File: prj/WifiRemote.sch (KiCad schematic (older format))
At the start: 68 parts, among them J1 DIP-BLACK-MALE-HEADER-VERT_4P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, J2 DIP-BLACK-MALE-HEADER_6P-2.54_, K1 DIP-SWITCH-TACTILE-SPST-NO_TS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, K2 DIP-SWITCH-TACTILE-SPST-NO_TS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, K3 DIP-SWITCH-TACTILE-SPST-NO_TS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, K4 DIP-SWITCH-TACTILE-SPST-NO_TS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, M1 Mechanical_Mount, M2 Mechanical_Mount, M3 Mechanical_Mount, M4 Mechanical_Mount, Q1 SMD-MOSFET-P-CH-20V-2A-FDN340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, SW1 DIP-TOGGLE-SWITCH-ON-ON_3+2P-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, U1 CONTROLLER-ESP8266, U2 BOOST-MCP1642B-ADJI/MC-MSOP8

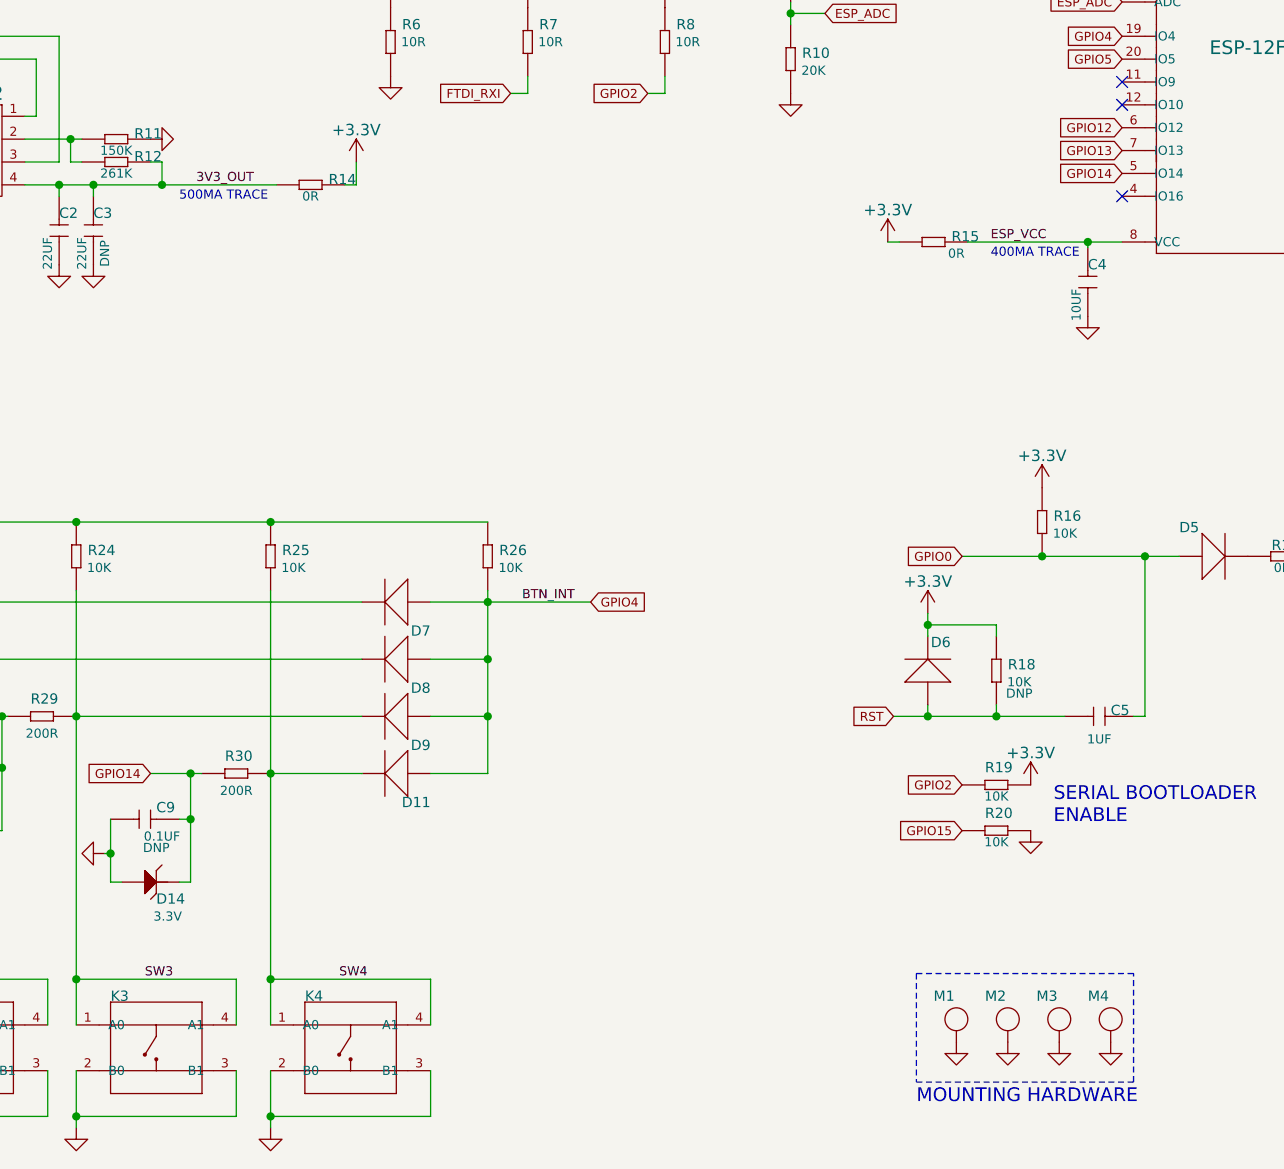
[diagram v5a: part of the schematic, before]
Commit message: Added mounting hole footprint
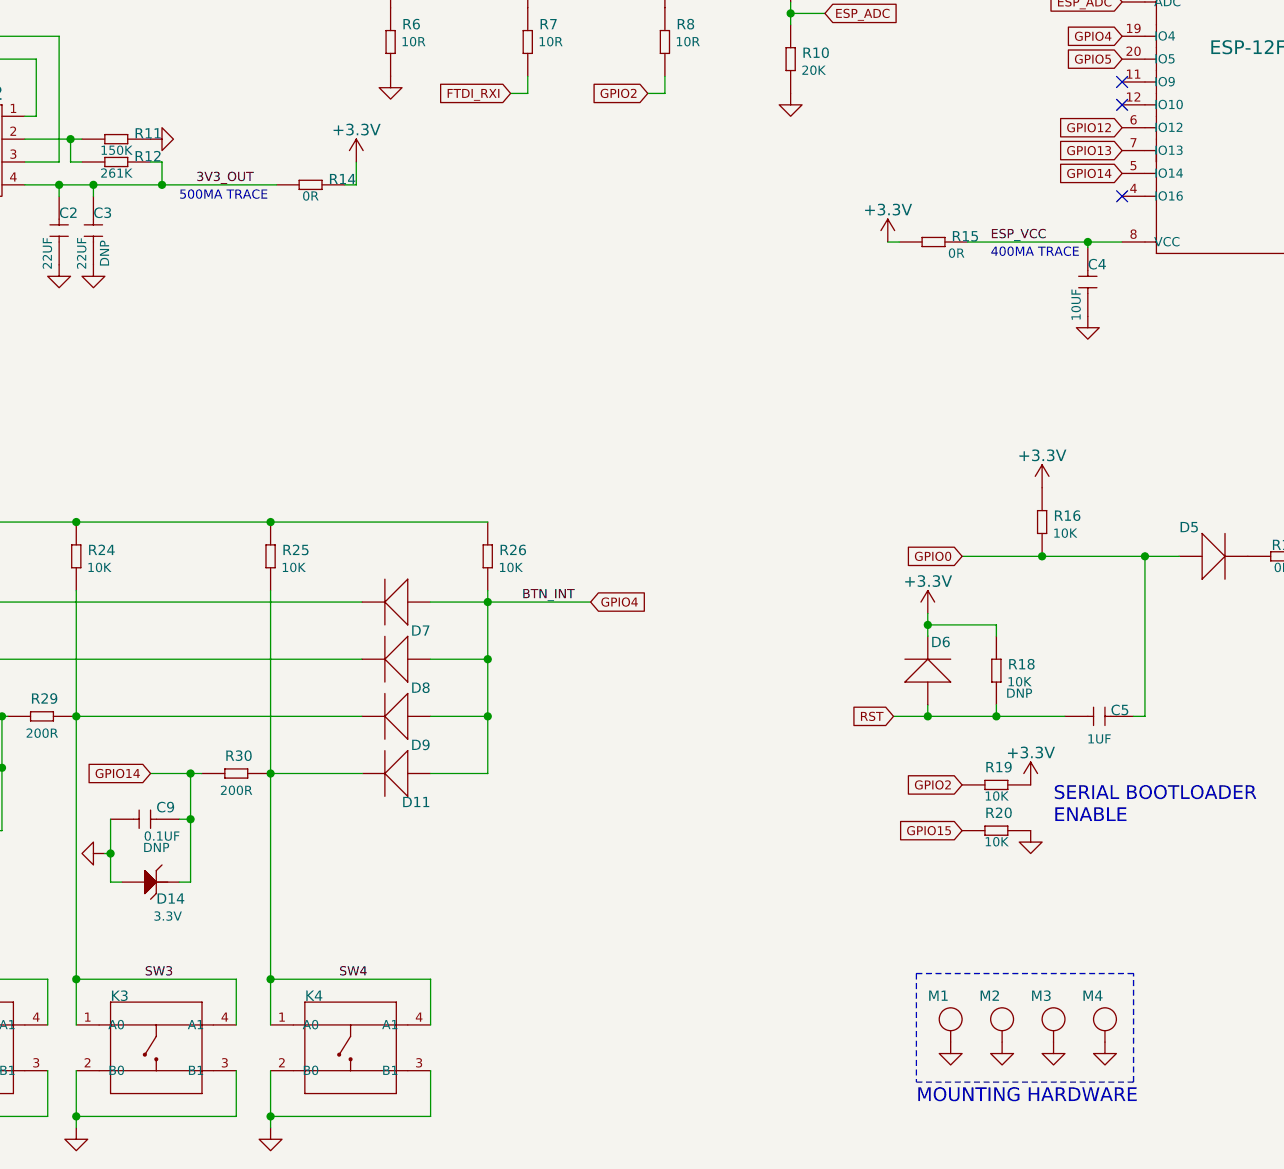
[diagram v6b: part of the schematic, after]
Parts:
- M1, M2, M3, M4: footprint (none) -> ICEE-Mechanical:mounting_panhead6
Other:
- moved on the sheet: M1, M2, M3, M4
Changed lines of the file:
@@
 	3750 2050 3800 2050
 Wire Wire Line
-	3800 2150 3800 2050
+	3800 2050 3800 2150
 Wire Wire Line
 	3500 2150 3500 2200
@@
 L Mechanical_Mount M1
 U 1 1 59BB9484
-P 7275 5800
-F 0 "M1" H 7175 5875 45  0000 L BNN
-F 1 "Mechanical_Mount" H 7075 5600 45  0001 L BNN
-F 2 "" H 7275 5800 60  0001 C CNN
-F 3 "" H 7275 5800 60  0001 C CNN
-	1    7275 5800
+P 7250 5800
+F 0 "M1" H 7150 5875 45  0000 L BNN
+F 1 "Mechanical_Mount" H 7050 5600 45  0001 L BNN
+F 2 "ICEE-Mechanical:mounting_panhead6" H 7250 5800 60  0001 C CNN
+F 3 "" H 7250 5800 60  0001 C CNN
+	1    7250 5800
 	1    0    0    -1
 $EndComp
@@
 L Mechanical_Mount M2
 U 1 1 59BB9AA5
-P 7500 5800
-F 0 "M2" H 7400 5875 45  0000 L BNN
-F 1 "Mechanical_Mount" H 7300 5600 45  0001 L BNN
-F 2 "" H 7500 5800 60  0001 C CNN
-F 3 "" H 7500 5800 60  0001 C CNN
-	1    7500 5800
+P 7475 5800
+F 0 "M2" H 7375 5875 45  0000 L BNN
+F 1 "Mechanical_Mount" H 7275 5600 45  0001 L BNN
+F 2 "ICEE-Mechanical:mounting_panhead6" H 7475 5800 60  0001 C CNN
+F 3 "" H 7475 5800 60  0001 C CNN
+	1    7475 5800
 	1    0    0    -1
 $EndComp
@@
 L Mechanical_Mount M3
 U 1 1 59BB9B95
-P 7725 5800
-F 0 "M3" H 7625 5875 45  0000 L BNN
-F 1 "Mechanical_Mount" H 7525 5600 45  0001 L BNN
-F 2 "" H 7725 5800 60  0001 C CNN
-F 3 "" H 7725 5800 60  0001 C CNN
-	1    7725 5800
-	1    0    0    -1
-$EndComp
-$Comp
-L GNDD #PWR?
+P 7700 5800
+F 0 "M3" H 7600 5875 45  0000 L BNN
+F 1 "Mechanical_Mount" H 7500 5600 45  0001 L BNN
+F 2 "ICEE-Mechanical:mounting_panhead6" H 7700 5800 60  0001 C CNN
+F 3 "" H 7700 5800 60  0001 C CNN
+	1    7700 5800
+	1    0    0    -1
+$EndComp
+$Comp
+L GNDD #PWR037
 U 1 1 59BC0554
-P 7275 5900
-F 0 "#PWR?" H 7275 5650 50  0001 C CNN
-F 1 "GNDD" H 7275 5750 50  0001 C CNN
-F 2 "" H 7275 5900 50  0000 C CNN
-F 3 "" H 7275 5900 50  0000 C CNN
-	1    7275 5900
-	1    0    0    -1
-$EndComp
-$Comp
-L GNDD #PWR?
+P 7250 5900
+F 0 "#PWR037" H 7250 5650 50  0001 C CNN
+F 1 "GNDD" H 7250 5750 50  0001 C CNN
+F 2 "" H 7250 5900 50  0000 C CNN
+F 3 "" H 7250 5900 50  0000 C CNN
+	1    7250 5900
+	1    0    0    -1
+$EndComp
+$Comp
+L GNDD #PWR038
 U 1 1 59BC09E3
-P 7500 5900
-F 0 "#PWR?" H 7500 5650 50  0001 C CNN
-F 1 "GNDD" H 7500 5750 50  0001 C CNN
-F 2 "" H 7500 5900 50  0000 C CNN
-F 3 "" H 7500 5900 50  0000 C CNN
-	1    7500 5900
-	1    0    0    -1
-$EndComp
-$Comp
-L GNDD #PWR?
+P 7475 5900
+F 0 "#PWR038" H 7475 5650 50  0001 C CNN
+F 1 "GNDD" H 7475 5750 50  0001 C CNN
+F 2 "" H 7475 5900 50  0000 C CNN
+F 3 "" H 7475 5900 50  0000 C CNN
+	1    7475 5900
+	1    0    0    -1
+$EndComp
+$Comp
+L GNDD #PWR039
 U 1 1 59BC0C67
-P 7950 5900
-F 0 "#PWR?" H 7950 5650 50  0001 C CNN
-F 1 "GNDD" H 7950 5750 50  0001 C CNN
-F 2 "" H 7950 5900 50  0000 C CNN
-F 3 "" H 7950 5900 50  0000 C CNN
-	1    7950 5900
+P 7925 5900
+F 0 "#PWR039" H 7925 5650 50  0001 C CNN
+F 1 "GNDD" H 7925 5750 50  0001 C CNN
+F 2 "" H 7925 5900 50  0000 C CNN
+F 3 "" H 7925 5900 50  0000 C CNN
+	1    7925 5900
 	1    0    0    -1
 $EndComp
@@
 L Mechanical_Mount M4
 U 1 1 59BBA5DF
-P 7950 5800
-F 0 "M4" H 7850 5875 45  0000 L BNN
-F 1 "Mechanical_Mount" H 7750 5600 45  0001 L BNN
-F 2 "" H 7950 5800 60  0001 C CNN
-F 3 "" H 7950 5800 60  0001 C CNN
-	1    7950 5800
-	1    0    0    -1
-$EndComp
-$Comp
-L GNDD #PWR?
+P 7925 5800
+F 0 "M4" H 7825 5875 45  0000 L BNN
+F 1 "Mechanical_Mount" H 7725 5600 45  0001 L BNN
+F 2 "ICEE-Mechanical:mounting_panhead6" H 7925 5800 60  0001 C CNN
+F 3 "" H 7925 5800 60  0001 C CNN
+	1    7925 5800
+	1    0    0    -1
+$EndComp
+$Comp
+L GNDD #PWR040
 U 1 1 59BC0B90
-P 7725 5900
-F 0 "#PWR?" H 7725 5650 50  0001 C CNN
-F 1 "GNDD" H 7725 5750 50  0001 C CNN
-F 2 "" H 7725 5900 50  0000 C CNN
-F 3 "" H 7725 5900 50  0000 C CNN
-	1    7725 5900
-	1    0    0    -1
-$EndComp
+P 7700 5900
+F 0 "#PWR040" H 7700 5650 50  0001 C CNN
+F 1 "GNDD" H 7700 5750 50  0001 C CNN
+F 2 "" H 7700 5900 50  0000 C CNN
+F 3 "" H 7700 5900 50  0000 C CNN
+	1    7700 5900
+	1    0    0    -1
+$EndComp

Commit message: Routing has begun
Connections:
- net +BATT: now also SW1.B; no longer SW1.A
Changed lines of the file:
@@
 F 5 "311030008" H 1280 1850 20  0001 C CNN "SKU"
 	1    1250 1700
-	1    0    0    -1
+	1    0    0    1
 $EndComp
 $Comp

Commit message: Swapped LED colors, changed mechanical mounts, fixed schematic TVS diode pins, edited button connections to ESP
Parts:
- removed D2: SMD-LED-CLEAR-GREEN_0805_, SeeedOPL-LED-2016:LED-0805, symbol SMD-LED-CLEAR-GREEN_0805_
- added D2: SMD-LED-CLEAR-BLUE_0805_, SeeedOPL-LED-2016:LED-0805, symbol SMD-LED-CLEAR-BLUE_0805_
- M1, M2, M3, M4: footprint ICEE-Mechanical:mounting_panhead6 -> ICEE-Mechanical:mounting_panhead6_5mm
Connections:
- net +3V3: now also D2.+
- net GPIO12: now also C6.2, D10.- (2), R27.1; no longer C7.2, D12.- (2), R28.1
- net GPIO5: now also C7.2, D12.- (2), R28.1; no longer C6.2, D10.- (2), R27.1
- net at R7.1: now also D2.-
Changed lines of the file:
@@
 Text GLabel 5675 3975 2    39   Input ~ 0
 GPIO4
+Text GLabel 2075 4225 0    39   Input ~ 0
+GPIO5
 Text GLabel 1325 3975 0    39   Input ~ 0
-GPIO5
-Text GLabel 2075 4225 0    39   Input ~ 0
 GPIO12
 Text GLabel 2950 4475 0    39   Input ~ 0
@@
 	1    8400 3775
 	1    0    0    -1
-$EndComp
-$Comp
-L SMD-LED-CLEAR-GREEN_0805_ D2
-U 1 1 59B368E9
-P 5400 1225
-F 0 "D2" V 5350 1225 45  0000 L BNN
-F 1 "SMD-LED-CLEAR-GREEN_0805_" H 5200 1025 45  0001 L BNN
-F 2 "SeeedOPL-LED-2016:LED-0805" H 5400 1225 60  0001 C CNN
-F 3 "" H 5400 1225 60  0000 C CNN
-F 4 "17-215SYGC_S530-E2_TR8" V 5500 1475 20  0000 C CNN "MPN"
-F 5 "304090057" H 5430 1375 20  0001 C CNN "SKU"
-	1    5400 1225
-	0    1    1    0
 $EndComp
 $Comp
@@
 F 0 "M1" H 7150 5875 45  0000 L BNN
 F 1 "Mechanical_Mount" H 7050 5600 45  0001 L BNN
-F 2 "ICEE-Mechanical:mounting_panhead6" H 7250 5800 60  0001 C CNN
+F 2 "ICEE-Mechanical:mounting_panhead6_5mm" H 7250 5800 60  0001 C CNN
 F 3 "" H 7250 5800 60  0001 C CNN
 	1    7250 5800
@@
 F 0 "M2" H 7375 5875 45  0000 L BNN
 F 1 "Mechanical_Mount" H 7275 5600 45  0001 L BNN
-F 2 "ICEE-Mechanical:mounting_panhead6" H 7475 5800 60  0001 C CNN
+F 2 "ICEE-Mechanical:mounting_panhead6_5mm" H 7475 5800 60  0001 C CNN
 F 3 "" H 7475 5800 60  0001 C CNN
 	1    7475 5800
@@
 F 0 "M3" H 7600 5875 45  0000 L BNN
 F 1 "Mechanical_Mount" H 7500 5600 45  0001 L BNN
-F 2 "ICEE-Mechanical:mounting_panhead6" H 7700 5800 60  0001 C CNN
+F 2 "ICEE-Mechanical:mounting_panhead6_5mm" H 7700 5800 60  0001 C CNN
 F 3 "" H 7700 5800 60  0001 C CNN
 	1    7700 5800
@@
 F 0 "M4" H 7825 5875 45  0000 L BNN
 F 1 "Mechanical_Mount" H 7725 5600 45  0001 L BNN
-F 2 "ICEE-Mechanical:mounting_panhead6" H 7925 5800 60  0001 C CNN
+F 2 "ICEE-Mechanical:mounting_panhead6_5mm" H 7925 5800 60  0001 C CNN
 F 3 "" H 7925 5800 60  0001 C CNN
 	1    7925 5800
@@
 Text Notes 7100 6175 0    60   ~ 0
 MOUNTING HARDWARE
+$Comp
+L SMD-LED-CLEAR-BLUE_0805_ D2
+U 1 1 59C1E2BF
+P 5400 1225
+F 0 "D2" V 5350 1250 45  0000 L BNN
+F 1 "SMD-LED-CLEAR-BLUE_0805_" H 5200 1025 45  0001 L BNN
+F 2 "SeeedOPL-LED-2016:LED-0805" H 5400 1225 60  0001 C CNN
+F 3 "" H 5400 1225 60  0001 C CNN
+F 4 "EL-17-215_BHC-AN1P2_3T" V 5500 1475 20  0000 C CNN "MPN"
+F 5 "304090061" H 5430 1375 20  0001 C CNN "SKU"
+	1    5400 1225
+	0    1    1    0
+$EndComp
 $EndSCHEMATC
